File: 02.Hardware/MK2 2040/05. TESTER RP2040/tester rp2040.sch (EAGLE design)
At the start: 59 parts, among them IC1 MAX4634EUB+T, J1 302-S201, Q1 PJA3416AE_R1_00001, Q2 2N7002PW, Q3 2N7002PW, Q4 RQ3G110ATTB, Q5 PJA3416AE_R1_00001, Q6 2N7002PW, Q7 RQ3G110ATTB, Q8 PJA3416AE_R1_00001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

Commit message: Revision de PCB (DGB)
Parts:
- R15, R28, R30: value (none) -> 100R
- R25, R26, R27: value (none) -> 2k2
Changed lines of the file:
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@@
 <part name="SUPPLY21" library="SparkFun-PowerSymbols" library_urn="urn:adsk.eagle:library:530" deviceset="VCC" device=""/>
 <part name="S1" library="SparkFun-Switches" library_urn="urn:adsk.eagle:library:535" deviceset="MOMENTARY-SWITCH-SPST" device="-SMD-5.2MM" package3d_urn="urn:adsk.eagle:package:40167/1"/>
-<part name="R25" library="SparkFun-Resistors" library_urn="urn:adsk.eagle:library:532" deviceset="RESISTOR" device="0805" package3d_urn="urn:adsk.eagle:package:39651/1" value=" "/>
+<part name="R25" library="SparkFun-Resistors" library_urn="urn:adsk.eagle:library:532" deviceset="RESISTOR" device="0805" package3d_urn="urn:adsk.eagle:package:39651/1" value="2k2"/>
 <part name="GND27" library="SparkFun" deviceset="GND" device=""/>
 <part name="C9" library="SparkFun-Passives" deviceset="CAP" device="0805" value="100n 50v X7R/X5R"/>
 <part name="GND28" library="SparkFun" deviceset="GND" device=""/>
 <part name="S2" library="SparkFun-Switches" library_urn="urn:adsk.eagle:library:535" deviceset="MOMENTARY-SWITCH-SPST" device="-SMD-5.2MM" package3d_urn="urn:adsk.eagle:package:40167/1"/>
-<part name="R26" library="SparkFun-Resistors" library_urn="urn:adsk.eagle:library:532" deviceset="RESISTOR" device="0805" package3d_urn="urn:adsk.eagle:package:39651/1" value=" "/>
+<part name="R26" library="SparkFun-Resistors" library_urn="urn:adsk.eagle:library:532" deviceset="RESISTOR" device="0805" package3d_urn="urn:adsk.eagle:package:39651/1" value="2k2"/>
 <part name="GND30" library="SparkFun" deviceset="GND" device=""/>
 <part name="C10" library="SparkFun-Passives" deviceset="CAP" device="0805" value="100n 50v X7R/X5R"/>
 <part name="GND31" library="SparkFun" deviceset="GND" device=""/>
 <part name="S3" library="SparkFun-Switches" library_urn="urn:adsk.eagle:library:535" deviceset="MOMENTARY-SWITCH-SPST" device="-SMD-5.2MM" package3d_urn="urn:adsk.eagle:package:40167/1"/>
-<part name="R27" library="SparkFun-Resistors" library_urn="urn:adsk.eagle:library:532" deviceset="RESISTOR" device="0805" package3d_urn="urn:adsk.eagle:package:39651/1" value=" "/>
+<part name="R27" library="SparkFun-Resistors" library_urn="urn:adsk.eagle:library:532" deviceset="RESISTOR" device="0805" package3d_urn="urn:adsk.eagle:package:39651/1" value="2k2"/>
 <part name="GND32" library="SparkFun" deviceset="GND" device=""/>
 <part name="C11" library="SparkFun-Passives" deviceset="CAP" device="0805" value="100n 50v X7R/X5R"/>
 <part name="GND33" library="SparkFun" deviceset="GND" device=""/>
-<part name="R28" library="SparkFun-Resistors" library_urn="urn:adsk.eagle:library:532" deviceset="RESISTOR" device="0805" package3d_urn="urn:adsk.eagle:package:39651/1" value=" "/>
-<part name="R30" library="SparkFun-Resistors" library_urn="urn:adsk.eagle:library:532" deviceset="RESISTOR" device="0805" package3d_urn="urn:adsk.eagle:package:39651/1" value=" "/>
-<part name="R15" library="SparkFun-Resistors" library_urn="urn:adsk.eagle:library:532" deviceset="RESISTOR" device="0805" package3d_urn="urn:adsk.eagle:package:39651/1" value=" "/>
+<part name="R28" library="SparkFun-Resistors" library_urn="urn:adsk.eagle:library:532" deviceset="RESISTOR" device="0805" package3d_urn="urn:adsk.eagle:package:39651/1" value="100R"/>
+<part name="R30" library="SparkFun-Resistors" library_urn="urn:adsk.eagle:library:532" deviceset="RESISTOR" device="0805" package3d_urn="urn:adsk.eagle:package:39651/1" value="100R"/>
+<part name="R15" library="SparkFun-Resistors" library_urn="urn:adsk.eagle:library:532" deviceset="RESISTOR" device="0805" package3d_urn="urn:adsk.eagle:package:39651/1" value="100R"/>
 <part name="U$3" library="SparkFun-Aesthetics" deviceset="VCC-ISO" device="" value="3V3"/>
 <part name="U$4" library="SparkFun-Aesthetics" deviceset="VCC-ISO" device="" value="3V3"/>
@@
 <wire x1="215.9" y1="121.92" x2="215.9" y2="144.78" width="0.1524" layer="91"/>
 <junction x="215.9" y="144.78"/>
+<junction x="180.34" y="137.16"/>
 </segment>
 </net>
@@
 <wire x1="177.8" y1="88.9" x2="215.9" y2="88.9" width="0.1524" layer="91"/>
 <wire x1="215.9" y1="88.9" x2="215.9" y2="106.68" width="0.1524" layer="91"/>
+<junction x="177.8" y="81.28"/>
 </segment>
 </net>
@@
 </sheet>
 </sheets>
+<errors>
+</errors>
 </schematic>
 </drawing>

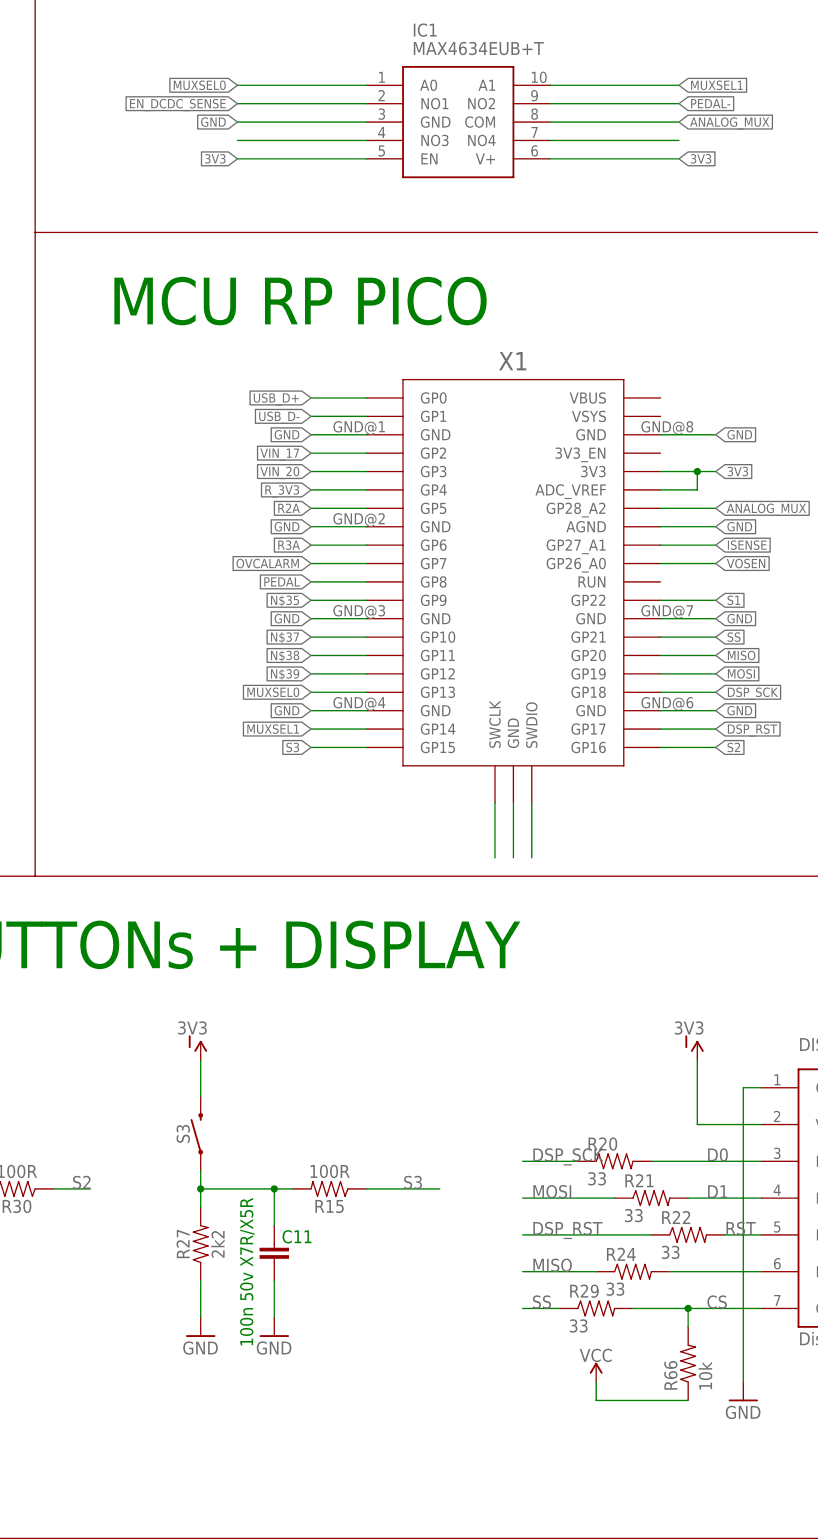
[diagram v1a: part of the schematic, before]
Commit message: Correccion Errores
Señal Vcc sin conectar.
Añadido sensado de señales VBUS_SENSE y OVC_ALARM.
Mejorado el Plano de GND para evitar estrangulamientos.
Ensanchadas las pistas que conectan con vias.
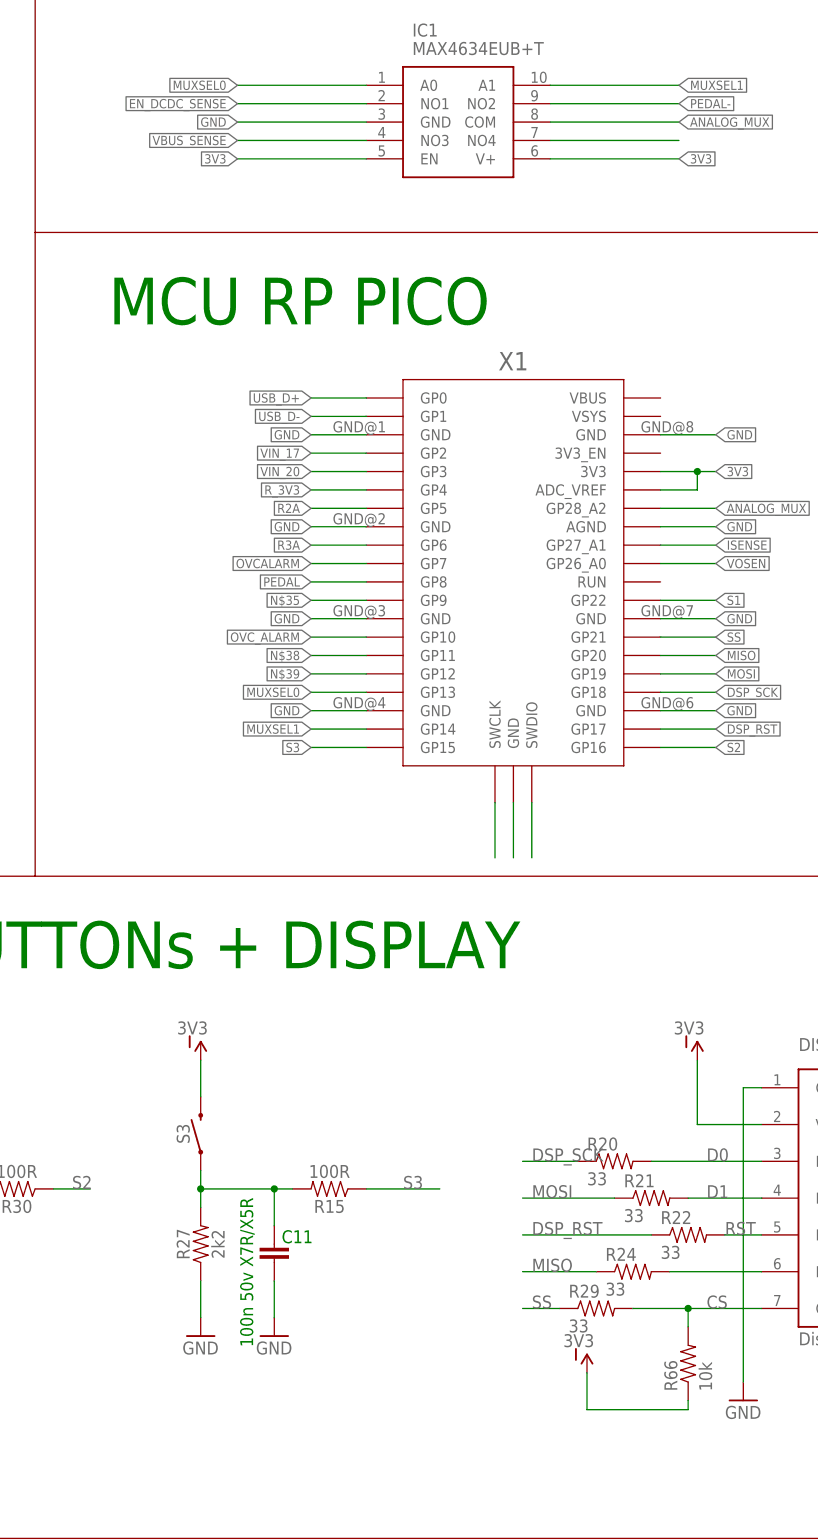
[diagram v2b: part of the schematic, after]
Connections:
- removed net N$37: X1.GP10
- removed net N$53: IC1.NO3
- removed net VCC: R66.1
- net 3V3: now also R66.1
- net OVC_ALARM: now also X1.GP10
- net VBUS_SENSE: now also IC1.NO3
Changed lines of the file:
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@@
 <part name="R24" library="SparkFun-Resistors" library_urn="urn:adsk.eagle:library:532" deviceset="RESISTOR" device="0805" package3d_urn="urn:adsk.eagle:package:39651/1" value="33"/>
 <part name="R29" library="SparkFun-Resistors" library_urn="urn:adsk.eagle:library:532" deviceset="RESISTOR" device="0805" package3d_urn="urn:adsk.eagle:package:39651/1" value="33"/>
-<part name="SUPPLY21" library="SparkFun-PowerSymbols" library_urn="urn:adsk.eagle:library:530" deviceset="VCC" device=""/>
 <part name="S1" library="SparkFun-Switches" library_urn="urn:adsk.eagle:library:535" deviceset="MOMENTARY-SWITCH-SPST" device="-SMD-5.2MM" package3d_urn="urn:adsk.eagle:package:40167/1"/>
 <part name="R25" library="SparkFun-Resistors" library_urn="urn:adsk.eagle:library:532" deviceset="RESISTOR" device="0805" package3d_urn="urn:adsk.eagle:package:39651/1" value="2k2"/>
@@
 <part name="U$5" library="SparkFun-Aesthetics" deviceset="VCC-ISO" device="" value="3V3"/>
 <part name="U$6" library="SparkFun-Aesthetics" deviceset="VCC-ISO" device="" value="3V3"/>
+<part name="U$7" library="SparkFun-Aesthetics" deviceset="VCC-ISO" device="" value="3V3"/>
 </parts>
 <sheets>
@@
 <attribute name="VALUE" x="-119.38" y="43.688" size="1.778" layer="96"/>
 </instance>
-<instance part="SUPPLY21" gate="G$1" x="-115.57" y="36.83" smashed="yes">
-<attribute name="VALUE" x="-115.57" y="39.624" size="1.778" layer="96" align="bottom-center"/>
-</instance>
 <instance part="S1" gate="G$1" x="-261.62" y="71.12" smashed="yes" rot="R90">
 <attribute name="NAME" x="-263.144" y="71.12" size="1.778" layer="95" font="vector" rot="R90" align="bottom-center"/>
@@
 <instance part="U$6" gate="G$1" x="-101.6" y="81.28" smashed="yes" rot="MR0">
 <attribute name="VALUE" x="-100.584" y="84.836" size="1.778" layer="96" rot="MR0"/>
+</instance>
+<instance part="U$7" gate="G$1" x="-116.84" y="38.1" smashed="yes" rot="MR0">
+<attribute name="VALUE" x="-115.824" y="41.656" size="1.778" layer="96" rot="MR0"/>
 </instance>
 </instances>
@@
 <label x="-264.16" y="149.86" size="1.778" layer="95"/>
 <pinref part="J1" gate="G$1" pin="7"/>
+</segment>
+<segment>
+<pinref part="X1" gate="G$1" pin="GP10"/>
+<wire x1="-147.32" y1="139.7" x2="-154.94" y2="139.7" width="0.1524" layer="91"/>
+<label x="-154.94" y="139.7" size="1.27" layer="95" rot="R180" xref="yes"/>
 </segment>
 </net>
@@
 <label x="-261.62" y="134.62" size="1.778" layer="95"/>
 </segment>
+<segment>
+<pinref part="IC1" gate="G$1" pin="NO3"/>
+<wire x1="-147.32" y1="208.28" x2="-165.1" y2="208.28" width="0.1524" layer="91"/>
+<label x="-165.1" y="208.28" size="1.27" layer="95" rot="R180" xref="yes"/>
+</segment>
 </net>
 <net name="VOUT" class="0">
@@
 <wire x1="-92.71" y1="72.39" x2="-101.6" y2="72.39" width="0.1524" layer="91"/>
 </segment>
+<segment>
+<pinref part="U$7" gate="G$1" pin="VCC-ISO"/>
+<wire x1="-116.84" y1="38.1" x2="-116.84" y2="33.02" width="0.1524" layer="91"/>
+<wire x1="-116.84" y1="33.02" x2="-102.87" y2="33.02" width="0.1524" layer="91"/>
+<pinref part="R66" gate="G$1" pin="1"/>
+<wire x1="-102.87" y1="33.02" x2="-102.87" y2="34.29" width="0.1524" layer="91"/>
+</segment>
 </net>
 <net name="N$35" class="0">
@@
 <wire x1="-147.32" y1="144.78" x2="-154.94" y2="144.78" width="0.1524" layer="91"/>
 <label x="-154.94" y="144.78" size="1.27" layer="95" rot="R180" xref="yes"/>
-</segment>
-</net>
-<net name="N$37" class="0">
-<segment>
-<pinref part="X1" gate="G$1" pin="GP10"/>
-<wire x1="-147.32" y1="139.7" x2="-154.94" y2="139.7" width="0.1524" layer="91"/>
-<label x="-154.94" y="139.7" size="1.27" layer="95" rot="R180" xref="yes"/>
 </segment>
 </net>
@@
 </segment>
 </net>
-<net name="N$53" class="0">
-<segment>
-<pinref part="IC1" gate="G$1" pin="NO3"/>
-<wire x1="-147.32" y1="208.28" x2="-165.1" y2="208.28" width="0.1524" layer="91"/>
-</segment>
-</net>
 <net name="MUXSEL1" class="0">
 <segment>
@@
 </segment>
 </net>
-<net name="VCC" class="0">
-<segment>
-<wire x1="-102.87" y1="34.29" x2="-115.57" y2="34.29" width="0.1524" layer="91"/>
-<wire x1="-115.57" y1="34.29" x2="-115.57" y2="36.83" width="0.1524" layer="91"/>
-<pinref part="R66" gate="G$1" pin="1"/>
-<pinref part="SUPPLY21" gate="G$1" pin="VCC"/>
-</segment>
-</net>

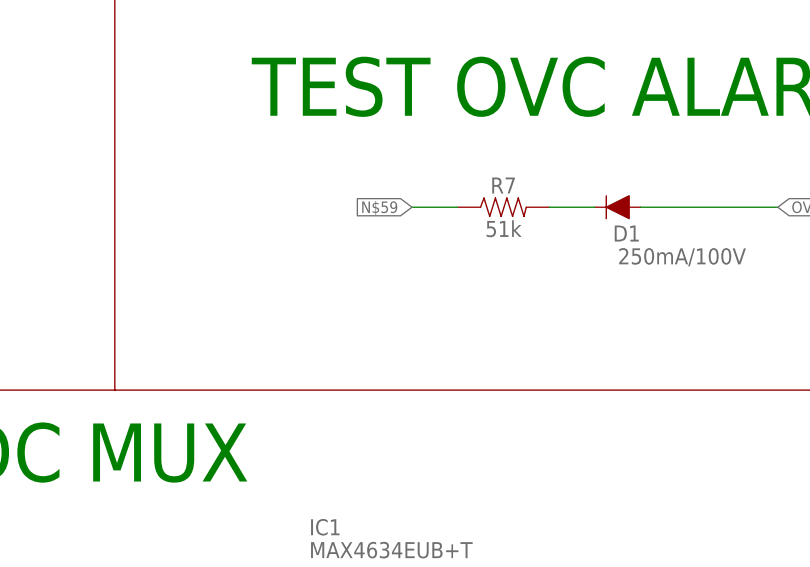
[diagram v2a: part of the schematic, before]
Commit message: Cambio de R7
El valor se cambia para tener en cuenta la R1 presente en la tarjeta cuando la señal OVC_ALARM es activada y prevenir la raspi de una subida de tension en la entrada digital.
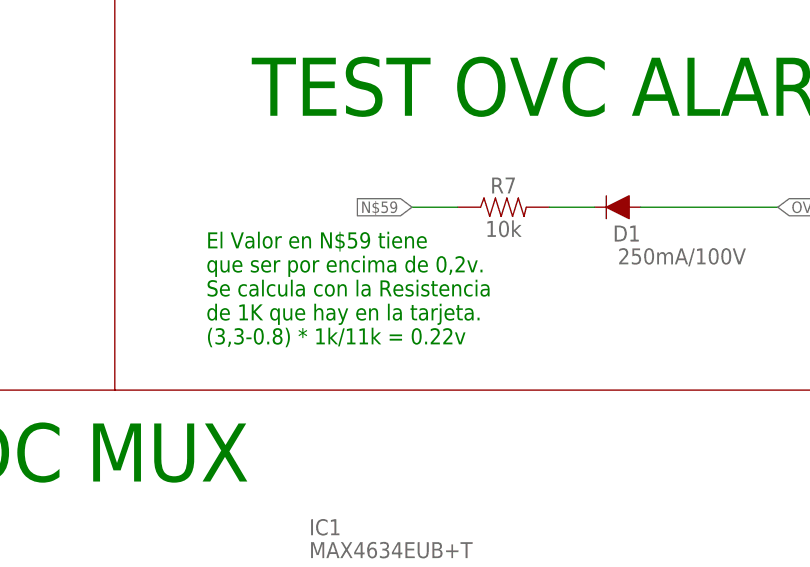
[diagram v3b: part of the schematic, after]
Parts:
- R7: value 51k -> 10k
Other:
- note added: "El Valor en N$59 tiene que ser por encima de 0,2v. Se calcula con la Resistencia de 1K que hay en la tarjeta. (3,3-0.8) * 1k/11k = 0.22v"
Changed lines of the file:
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@@
 <part name="R6" library="SparkFun-Resistors" library_urn="urn:adsk.eagle:library:532" deviceset="RESISTOR" device="0805" package3d_urn="urn:adsk.eagle:package:39651/1" value="47K"/>
 <part name="D1" library="SparkFun-DiscreteSemi" library_urn="urn:adsk.eagle:library:514" deviceset="DIODE" device="-BAS16J" package3d_urn="urn:adsk.eagle:package:38441/1" value="250mA/100V"/>
-<part name="R7" library="SparkFun-Resistors" library_urn="urn:adsk.eagle:library:532" deviceset="RESISTOR" device="0805" package3d_urn="urn:adsk.eagle:package:39651/1" value="51k"/>
+<part name="R7" library="SparkFun-Resistors" library_urn="urn:adsk.eagle:library:532" deviceset="RESISTOR" device="0805" package3d_urn="urn:adsk.eagle:package:39651/1" value="10k"/>
 <part name="J5" library="SparkFun-Connectors" library_urn="urn:adsk.eagle:library:513" deviceset="CONN_01" device="" package3d_urn="urn:adsk.eagle:package:38028/1"/>
 <part name="R31" library="SparkFun-Resistors" library_urn="urn:adsk.eagle:library:532" deviceset="RESISTOR" device="0805" package3d_urn="urn:adsk.eagle:package:39651/1" value="330R"/>
@@
 CONNECTORS</text>
 <text x="-208.28" y="93.98" size="6.4516" layer="91">BUTTONs + DISPLAY</text>
+<text x="-152.4" y="243.84" size="1.778" layer="91">El Valor en N$59 tiene
+que ser por encima de 0,2v.
+Se calcula con la Resistencia
+de 1K que hay en la tarjeta.
+(3,3-0.8) * 1k/11k = 0.22v</text>
 </plain>
 <instances>
